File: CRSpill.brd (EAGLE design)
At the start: 70 x 22.2 mm, 23 parts, among them IC1 7805DT, IC2 BLUE_PILL, IC3 NCV7351D1E, J3 MA04-1, SW1 SWITCH_TACTILETOP, U1 STM32F103C8, U7 XC6206, X1 8P8C-LED

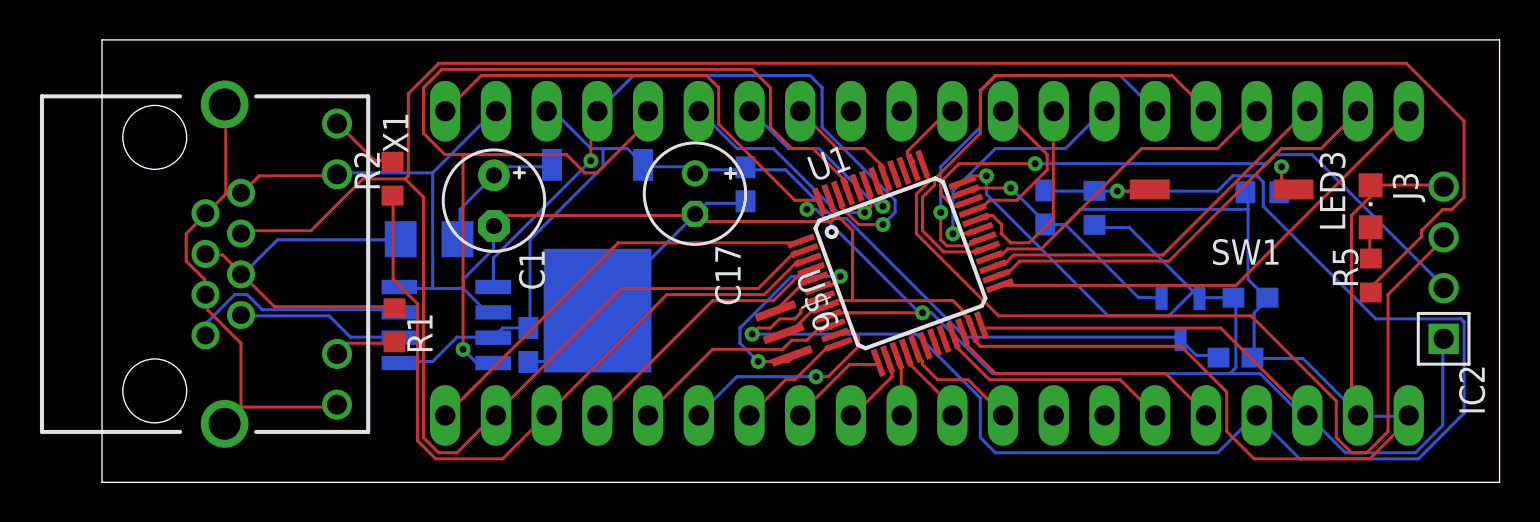
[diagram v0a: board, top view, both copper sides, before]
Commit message: 5V12Vの配線を強化
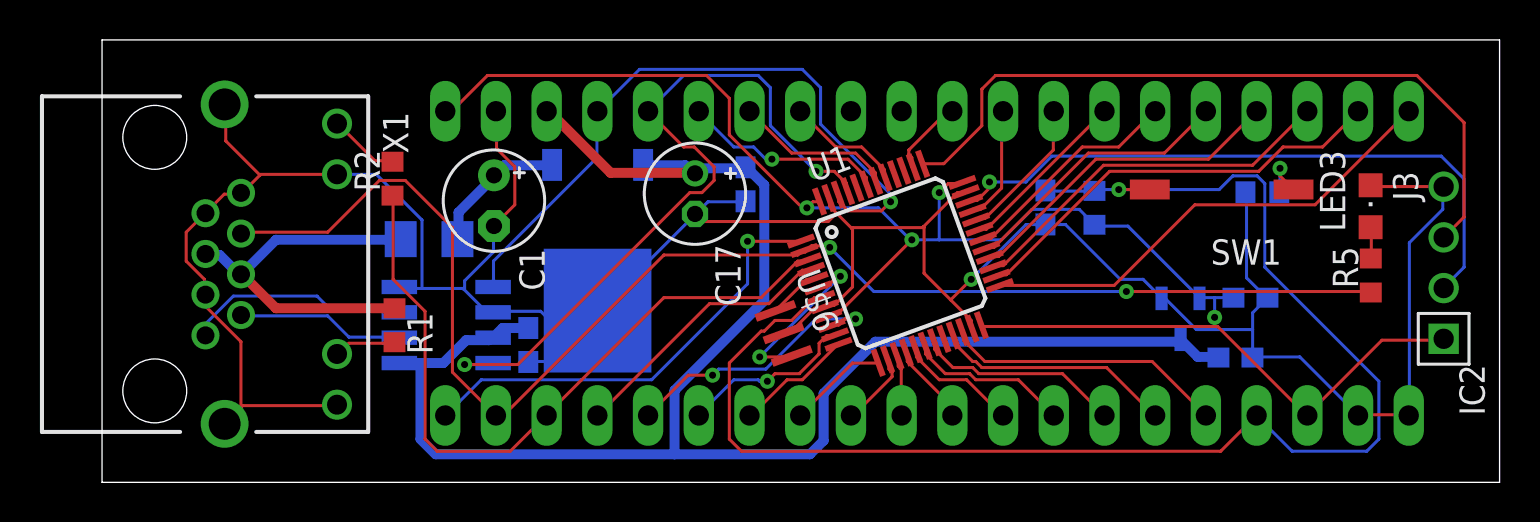
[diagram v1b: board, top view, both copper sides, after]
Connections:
- removed net LED0: IC2.P$13
- removed net LED1: IC2.P$14
- net PB0: now also IC2.P$13
- net PB1: now also IC2.P$14
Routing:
- net !EMS: track 116.2 -> 71.4 mm, vias 0 -> 2
- net +3V3: track 116.6 -> 85.6 mm, vias 3 -> 4
- net GND: track 185.6 -> 156.2 mm
- net +5V: track 56.8 -> 86.2 mm
- net CANRX: track 53.1 -> 37.4 mm, vias 1 -> 2
- net PA8: track 24.3 -> 13.9 mm
- net PB1: track 0.00 -> 10.2 mm
- net PA9: track 20.5 -> 11.3 mm, vias 1 -> 0
- net PB0: track 0.00 -> 8.12 mm
- net SWCLK: track 44.4 -> 37.2 mm
- net !RESET: track 77.5 -> 72.5 mm, vias 2 -> 1
- net PA10: track 12.8 -> 8.71 mm, vias 1 -> 0
- net PA11: track 10.7 -> 7.28 mm
- net N$11: track 11.4 -> 8.72 mm
- net PA12: track 8.45 -> 5.84 mm
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
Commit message: 未接続部を処理
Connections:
- removed net BP3: IC2.P$31
- removed net BP4: IC2.P$32
- net PB3: now also IC2.P$31
- net PB4: now also IC2.P$32
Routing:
- net PB4: track 0.00 -> 4.05 mm
- net PB3: track 0.00 -> 3.11 mm
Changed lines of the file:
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@@
 <signal name="PB3">
 <contactref element="U1" pad="39"/>
+<contactref element="IC2" pad="P$31"/>
+<wire x1="40.005" y1="16.6116" x2="40.005" y2="16.1544" width="0.1524" layer="1"/>
+<wire x1="39.8526" y1="16.764" x2="40.005" y2="16.6116" width="0.1524" layer="1"/>
+<wire x1="39.8526" y1="18.9738" x2="39.8526" y2="16.764" width="0.1524" layer="1"/>
+<wire x1="39.9288" y1="19.05" x2="39.8526" y2="18.9738" width="0.1524" layer="1"/>
+<wire x1="40.005" y1="16.1544" x2="40.063775" y2="16.1092125" width="0.1524" layer="1"/>
+<wire x1="39.9288" y1="19.05" x2="39.95" y2="19.09" width="0.1524" layer="1"/>
 </signal>
 <signal name="PB4">
 <contactref element="U1" pad="40"/>
+<contactref element="IC2" pad="P$32"/>
+<wire x1="39.5478" y1="16.383" x2="39.5478" y2="16.002" width="0.1524" layer="1"/>
+<wire x1="37.4142" y1="18.5166" x2="39.5478" y2="16.383" width="0.1524" layer="1"/>
+<wire x1="37.4142" y1="19.05" x2="37.4142" y2="18.5166" width="0.1524" layer="1"/>
+<wire x1="39.5478" y1="16.002" x2="39.593928125" y2="15.938203125" width="0.1524" layer="1"/>
+<wire x1="37.4142" y1="19.05" x2="37.41" y2="19.09" width="0.1524" layer="1"/>
 </signal>
 <signal name="PC15">
@@
 <wire x1="55.1688" y1="19.05" x2="55.19" y2="19.09" width="0.1524" layer="1"/>
 </signal>
-<signal name="BP4">
-<contactref element="IC2" pad="P$32"/>
-</signal>
-<signal name="BP3">
-<contactref element="IC2" pad="P$31"/>
-</signal>
 </signals>
